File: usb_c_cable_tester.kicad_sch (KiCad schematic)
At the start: 58 parts, among them J1 USB_C_Receptacle, J2 USB_C_Receptacle_ALLPINS, J3 USB_B_Micro, J4 USB3_B, J5 USB_B_Mini, J6 USB3_A

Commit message: Moved from https://github.com/SmittyHalibut/usb_c_cable_tester/tree/v2.2-jlcpcb #32
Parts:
- BT1: Alt LCSC (none) -> C70377; LCSC C70377 -> C7498148
- D1, D10, D11, D12, D13, D14, D15, D16, D17, D18, D19, D2, D20, D21, D22, D23, D24, D25, D3, D4, D5, D6, D7, D8, D9: Alt LCSC (none) -> C72038; LCSC C72038 -> C2286
- J1: value USB_C_Receptacle -> USB C; footprint easyeda:USB-C-SMD_UT11113-11602-7H -> Libraries:USB_C_Receptacle_24P_QCHT_C456013; Alt LCSC (none) -> C2761408; LCSC C2761408 -> C456013
- J2: value USB_C_Receptacle_ALLPINS -> USB C; footprint easyeda:USB-C-SMD_UT11113-11602-7H -> Libraries:USB_C_Receptacle_24P_QCHT_C456013; Alt LCSC (none) -> C2761408; LCSC C2761408 -> C456013
- J3: LCSC C132563 -> C404969
- J4: LCSC C70377 -> C105423

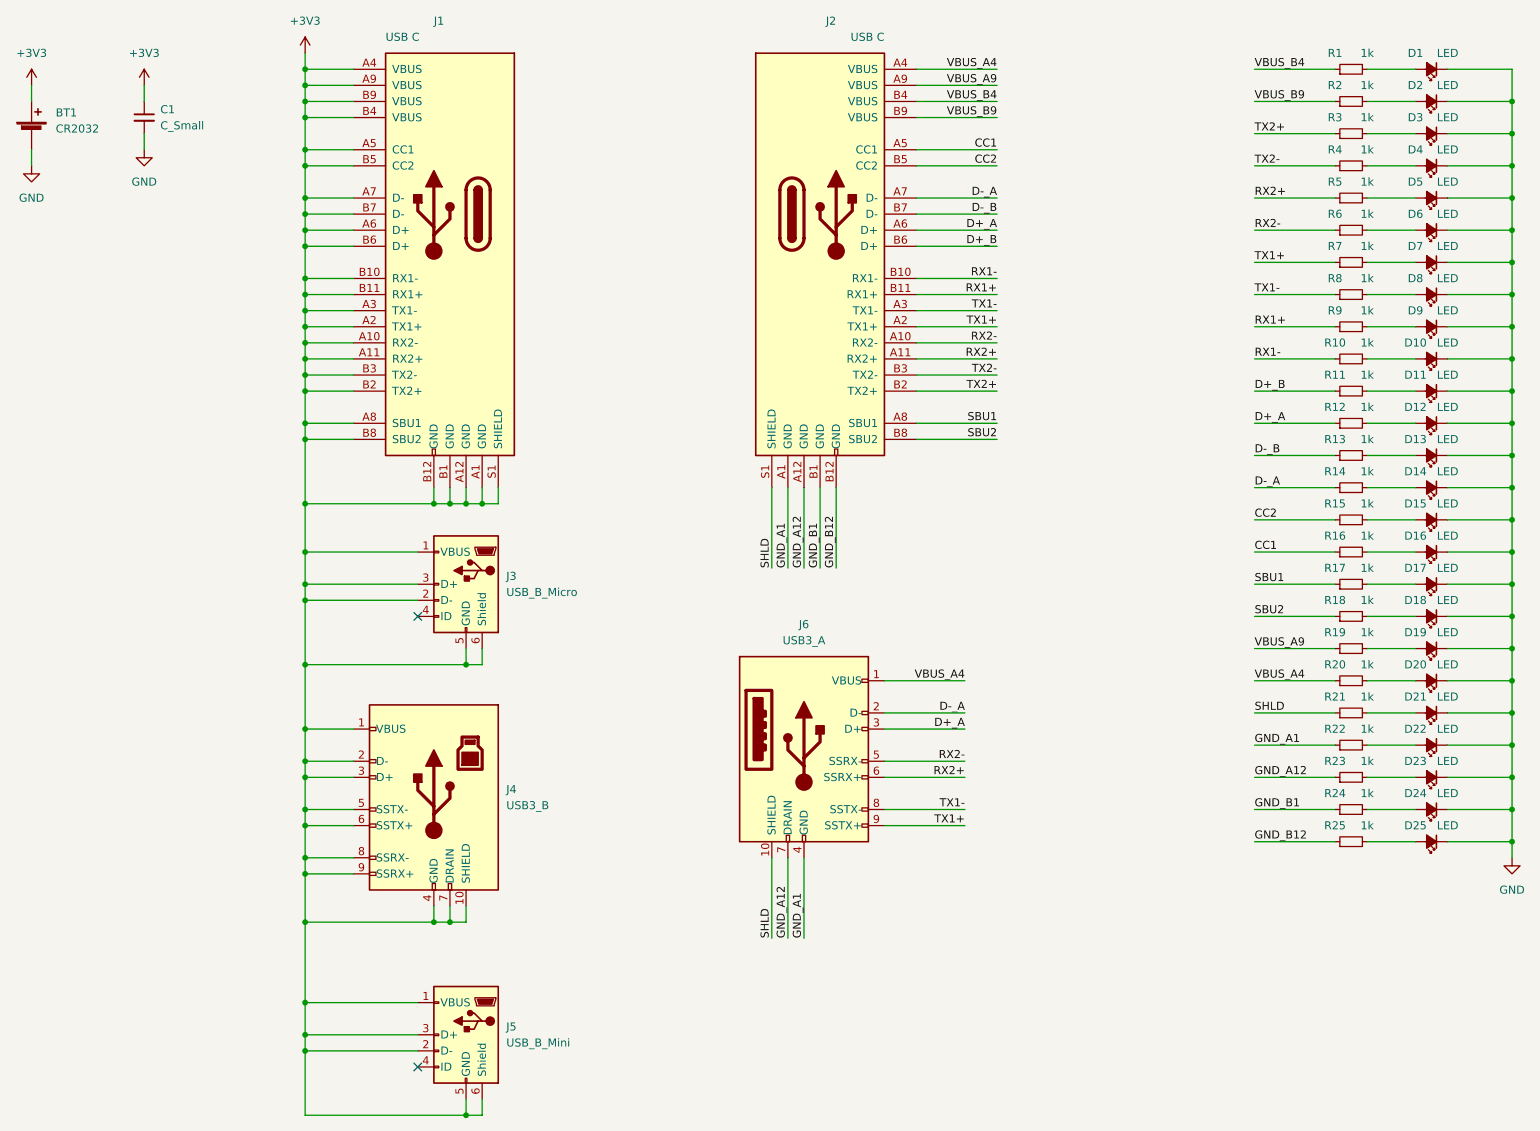
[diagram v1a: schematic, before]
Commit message: Revert "Merging changes for current (2026 May) JLCPCB stock and ordering."
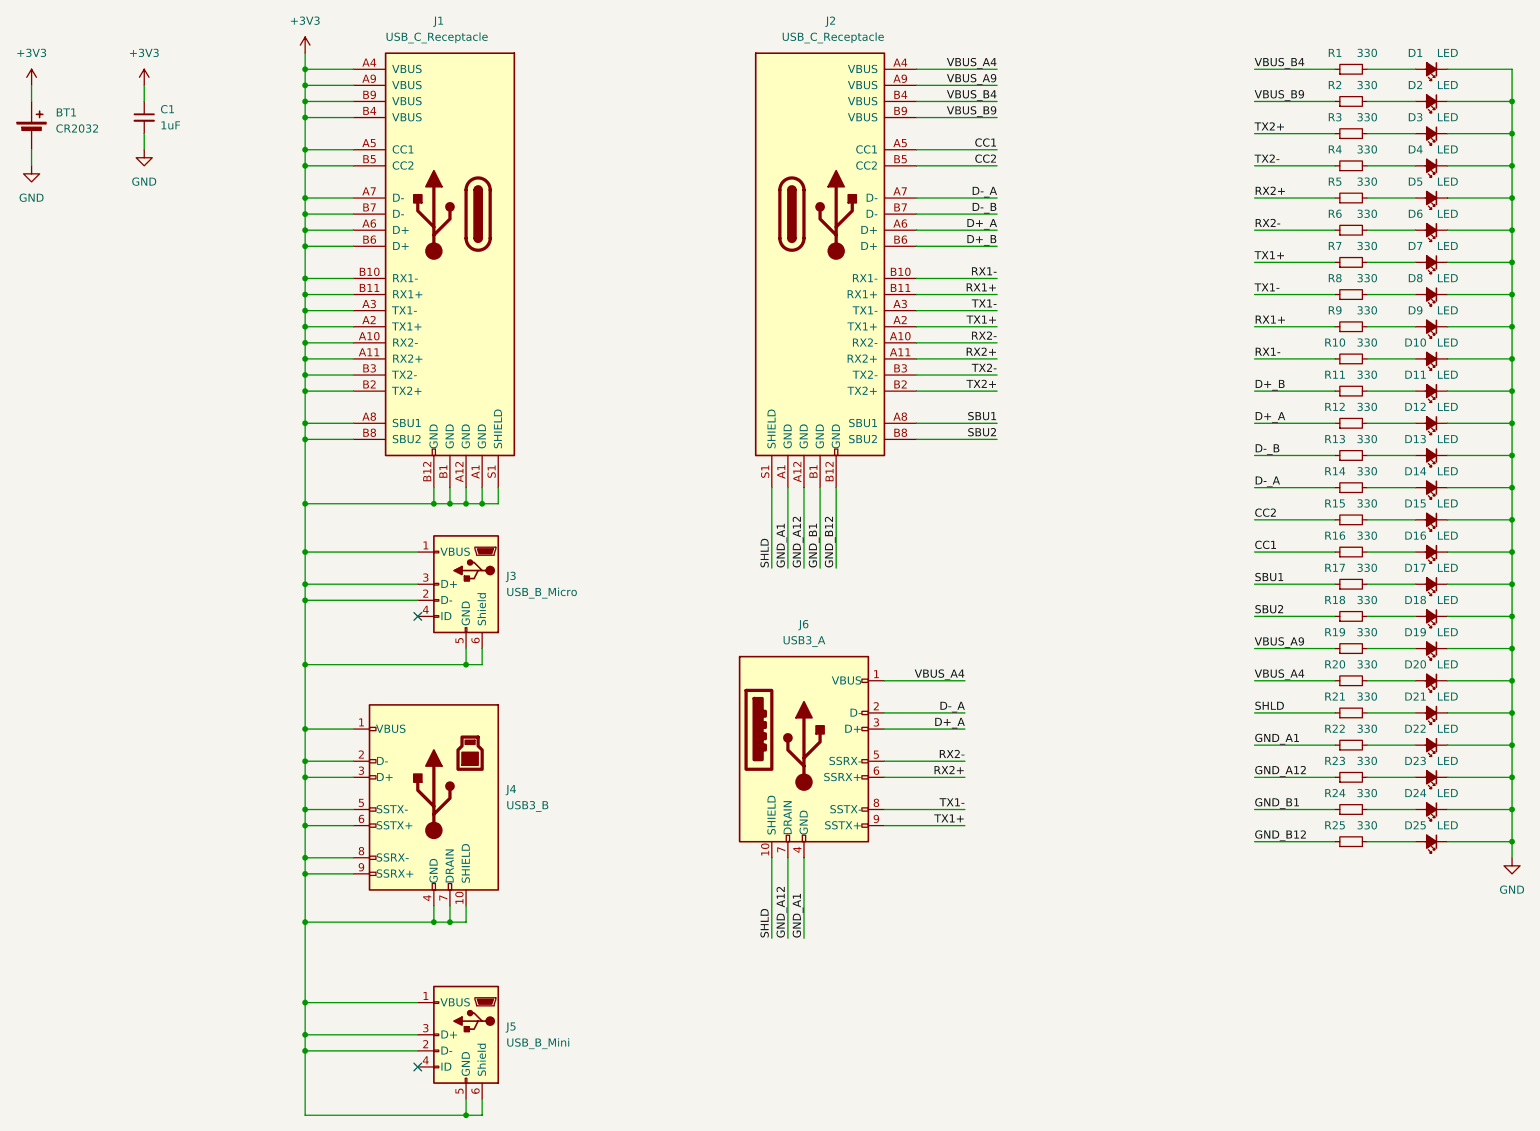
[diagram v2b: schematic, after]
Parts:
- BT1: footprint easyeda:BAT-TH_CR2032-BS-6-1 -> snapeda:BAT_BU2032SM-BT-GTR; Alt LCSC C70377 -> (none); LCSC C7498148 -> (none); MPN (none) -> BU2032SM-BT-GTR; Manufacturer (none) -> Memory Protection Devices
- C1: value C_Small -> 1uF; LCSC C15850 -> (none)
- D1, D10, D11, D12, D13, D14, D15, D16, D17, D18, D19, D2, D20, D21, D22, D23, D24, D25, D3, D4, D5, D6, D7, D8, D9: Alt LCSC C72038 -> (none); LCSC C2286 -> (none)
- J1, J2: value USB C -> USB_C_Receptacle; footprint Libraries:USB_C_Receptacle_24P_QCHT_C456013 -> snapeda:BELFUSE_SS-52400-003; Alt LCSC C2761408 -> (none); LCSC C456013 -> (none); MPN (none) -> SS-52400-003; Manufacturer (none) -> Stewart Connector
- J3: footprint easyeda:MICRO-USB-SMD_10118194-0001LF -> snapeda:AMPHENOL_10118194-0001LF_MOD; LCSC C404969 -> (none); MPN (none) -> 10118194-0001LF; Manufacturer (none) -> Amphenol ICC
- J4: footprint easyeda:USB-B-TH_XUNPU_USB-306BWD-ARW -> snapeda:AMPHENOL_GSB3211311WEU; ALT MPN (none) -> E8199-030-03; ALT Manufacturer (none) -> Pulse Electronics; LCSC C105423 -> (none); MPN (none) -> GSB3211311WEU; Manufacturer (none) -> Amphenol ICC
- J5: footprint easyeda:MINI-USB-SMD_MINI-5PTP -> snapeda:TE_1734510-1; ALT MPN (none) -> 0548190519; ALT Manufacturer (none) -> Molex; LCSC C2681563 -> (none); MPN (none) -> 1734510-1; Manufacturer (none) -> TE Connectivity
- J6: footprint easyeda:USB-A-TH_U231-091N-5 -> snapeda:AMPHENOL_GSB311131HR; ALT MPN (none) -> SS-52000-001; ALT Manufacturer (none) -> Stewart Connector; LCSC C381137 -> (none); MPN (none) -> GSB311131HR; Manufacturer (none) -> Amphenol ICC
- R1, R10, R11, R12, R13, R14, R15, R16, R17, R18, R19, R2, R20, R21, R22, R23, R24, R25, R3, R4, R5, R6, R7, R8, R9: value 1k -> 330; LCSC C4190 -> (none)
